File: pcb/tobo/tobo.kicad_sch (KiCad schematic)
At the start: 88 parts, among them J1 54548-2272, J2 Conn_01x02_Pin, J4 54548-2472, J5 Conn_01x09_Pin, J6 Conn_01x09_Pin, J7 Conn_01x09_Pin, J8 Hroparts Elec TYPE-C-31-M-12, U1 TS5A23167DCUR, U10 5015, U11 5015, U12 5015, U13 5015, U14 CH340E, U15 5015, U16 5015, U2 ATmega328P-AN, U3 TS5A23167DCUR, U4 TS5A23167DCUR, U5 TS5A23167DCUR, U6 5015, U7 5015, U8 5015, U9 5015, X1 TestPoint, X2 TestPoint, X7 TestPoint, Y4 TestPoint

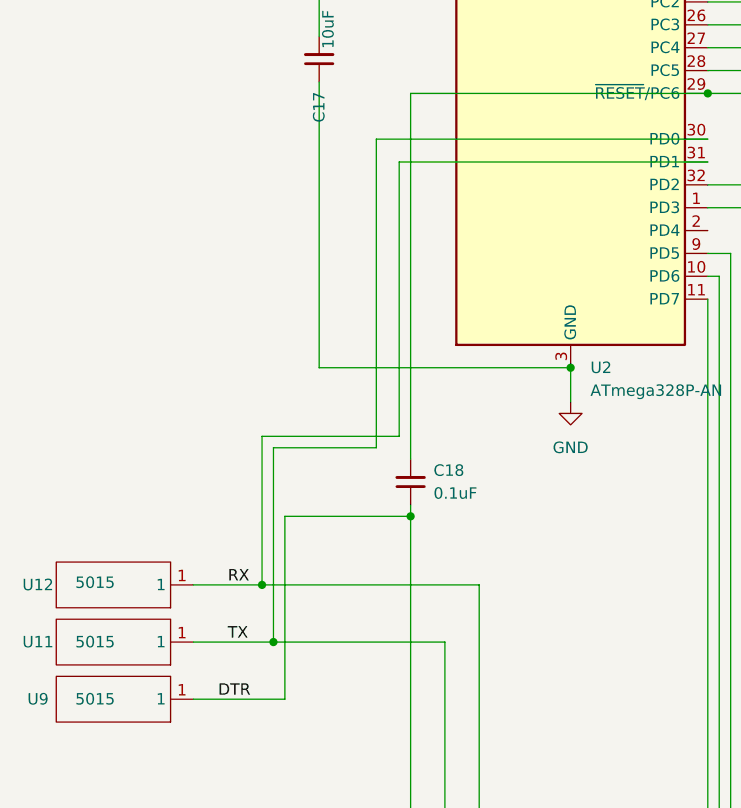
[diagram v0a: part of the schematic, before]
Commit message: Solution to the PCB error in v0.3a
If you've got a v0.4 board, no need to futz around with RX/TX.
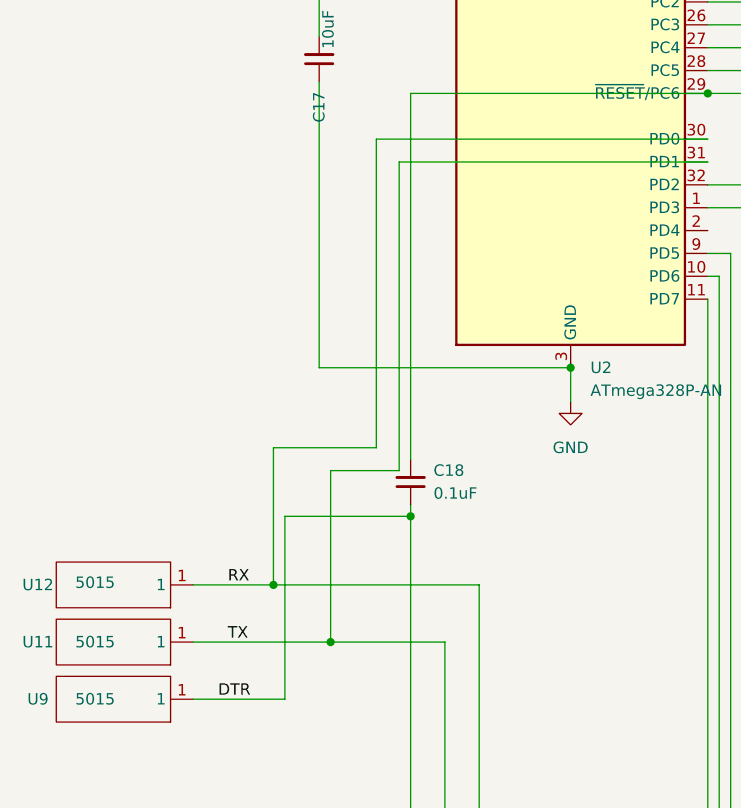
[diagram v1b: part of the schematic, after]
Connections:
- net RX: now also U2.30 (PD0); no longer U2.31 (PD1)
- net TX: now also U2.31 (PD1); no longer U2.30 (PD0)
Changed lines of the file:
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@@
+	)
+	(junction
+		(at 48.26 171.45)
+		(diameter 0)
+		(color 0 0 0 0)
 	)
 	(junction
@@
 	)
 	(junction
+		(at 41.91 165.1)
+		(diameter 0)
+		(color 0 0 0 0)
+	)
+	(junction
 		(at 331.47 201.93)
 		(diameter 0)
@@
 	)
 	(junction
-		(at 40.64 165.1)
-		(diameter 0)
-		(color 0 0 0 0)
-	)
-	(junction
 		(at 107.95 204.47)
 		(diameter 0)
@@
 		(color 0 0 0 0)
 	)
-	(junction
-		(at 41.91 171.45)
-		(diameter 0)
-		(color 0 0 0 0)
-	)
 	(wire
 		(pts
@@
 	(wire
 		(pts
-			(xy 40.64 148.59) (xy 40.64 165.1)
-		)
-		(stroke
-			(width 0)
-			(type default)
-		)
-	)
-	(wire
-		(pts
 			(xy 132.08 172.72) (xy 132.08 196.85)
 		)
@@
 	(wire
 		(pts
+			(xy 48.26 171.45) (xy 60.96 171.45)
+		)
+		(stroke
+			(width 0)
+			(type default)
+		)
+	)
+	(wire
+		(pts
 			(xy 327.66 170.18) (xy 327.66 187.96)
 		)
@@
 	(wire
 		(pts
-			(xy 40.64 148.59) (xy 55.88 148.59)
-		)
-		(stroke
-			(width 0)
-			(type default)
-		)
-	)
-	(wire
-		(pts
 			(xy 217.17 73.66) (xy 217.17 76.2)
 		)
@@
 	(wire
 		(pts
+			(xy 41.91 165.1) (xy 64.77 165.1)
+		)
+		(stroke
+			(width 0)
+			(type default)
+		)
+	)
+	(wire
+		(pts
 			(xy 186.69 63.5) (xy 189.23 63.5)
 		)
@@
 	(wire
 		(pts
-			(xy 41.91 171.45) (xy 60.96 171.45)
-		)
-		(stroke
-			(width 0)
-			(type default)
-		)
-	)
-	(wire
-		(pts
 			(xy 194.31 63.5) (xy 196.85 63.5)
 		)
@@
 	(wire
 		(pts
-			(xy 33.02 171.45) (xy 41.91 171.45)
+			(xy 33.02 171.45) (xy 48.26 171.45)
 		)
 		(stroke
@@
 	(wire
 		(pts
-			(xy 40.64 165.1) (xy 64.77 165.1)
+			(xy 33.02 165.1) (xy 41.91 165.1)
 		)
 		(stroke
@@
 	(wire
 		(pts
-			(xy 55.88 118.11) (xy 55.88 148.59)
+			(xy 55.88 118.11) (xy 55.88 152.4)
 		)
 		(stroke
@@
 	(wire
 		(pts
+			(xy 41.91 149.86) (xy 41.91 165.1)
+		)
+		(stroke
+			(width 0)
+			(type default)
+		)
+	)
+	(wire
+		(pts
 			(xy 137.16 100.33) (xy 110.49 100.33)
 		)
@@
 	(wire
 		(pts
-			(xy 33.02 165.1) (xy 40.64 165.1)
-		)
-		(stroke
-			(width 0)
-			(type default)
-		)
-	)
-	(wire
-		(pts
 			(xy 254 93.98) (xy 274.32 93.98)
 		)
@@
 	(wire
 		(pts
+			(xy 48.26 152.4) (xy 48.26 171.45)
+		)
+		(stroke
+			(width 0)
+			(type default)
+		)
+	)
+	(wire
+		(pts
 			(xy 134.62 228.6) (xy 134.62 237.49)
 		)
@@
 	(wire
 		(pts
-			(xy 41.91 149.86) (xy 41.91 171.45)
-		)
-		(stroke
-			(width 0)
-			(type default)
-		)
-	)
-	(wire
-		(pts
 			(xy 223.52 140.97) (xy 223.52 149.86)
 		)
@@
 		)
 		(stroke
+			(width 0)
+			(type default)
+		)
+	)
+	(wire
+		(pts
+			(xy 55.88 152.4) (xy 48.26 152.4)
+		)
+		(stroke

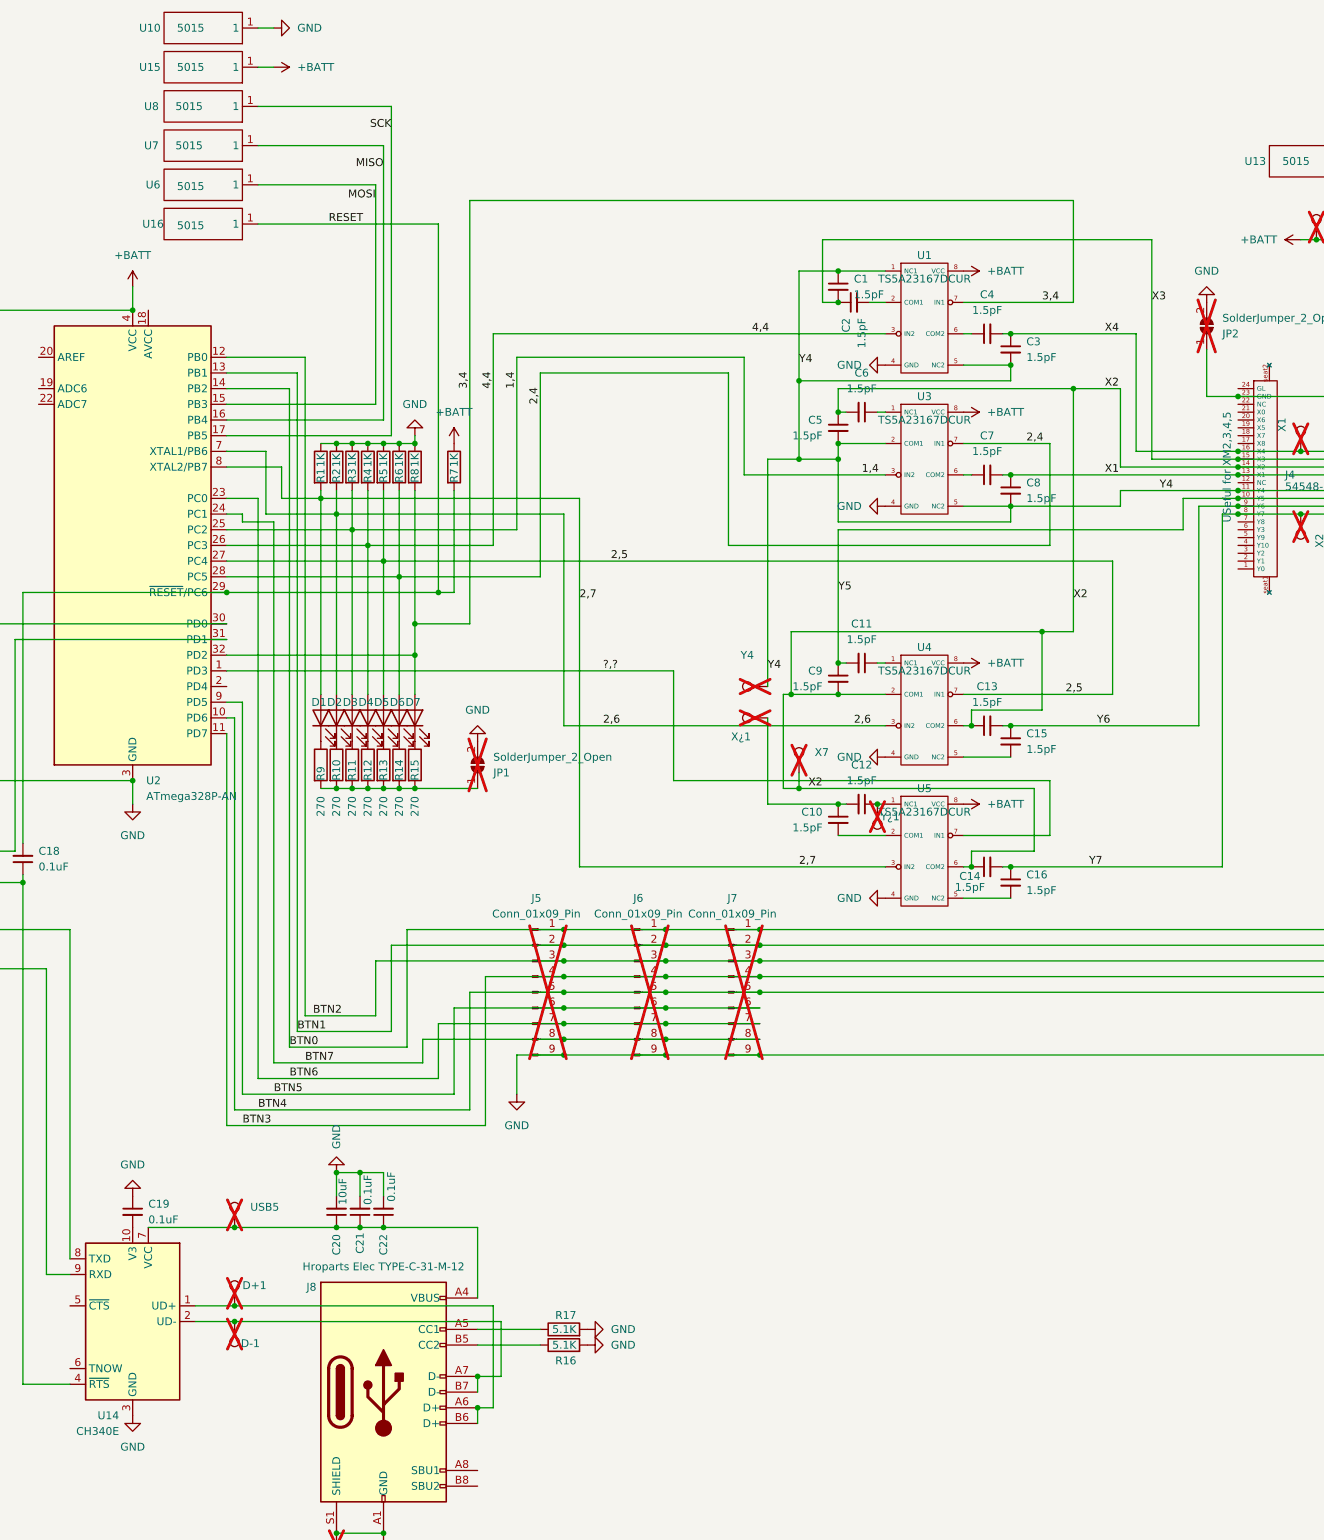
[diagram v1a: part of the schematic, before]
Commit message: PCB: Bump to Kicad 9 and preparation for step-up transformer
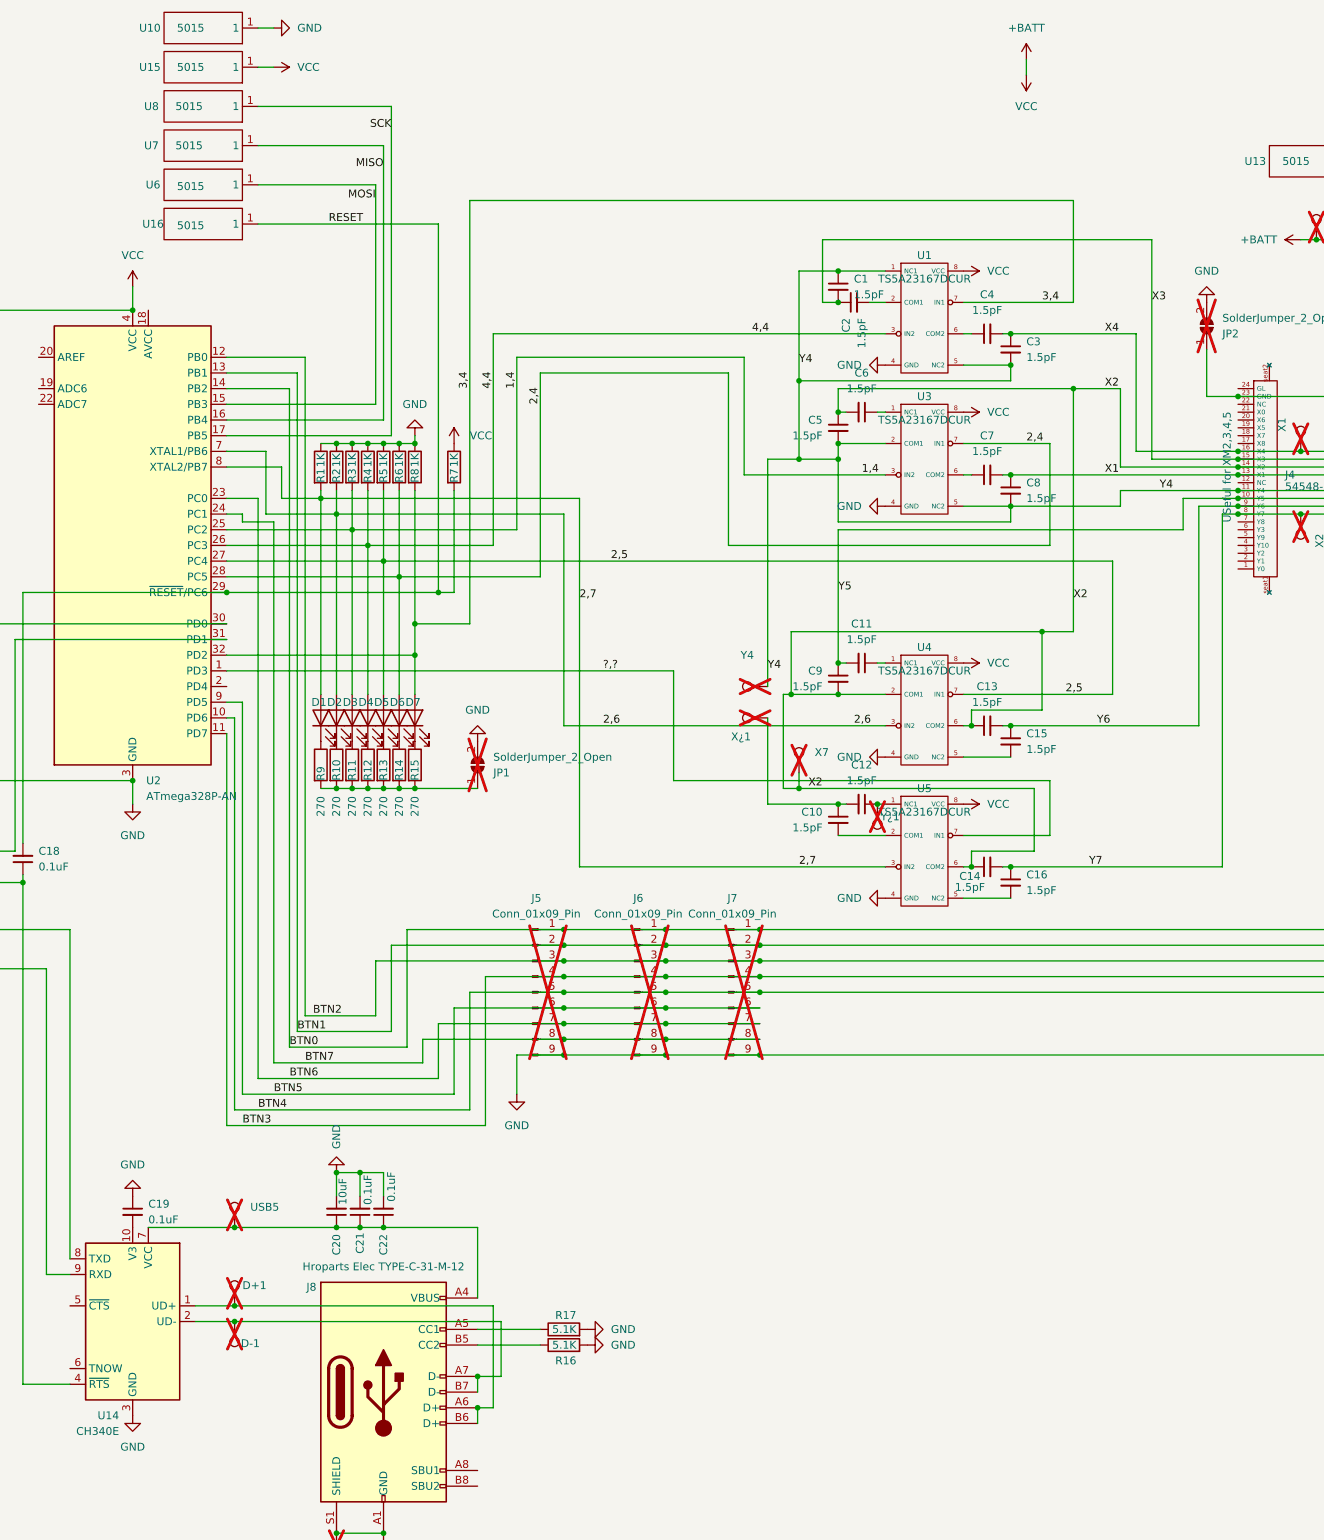
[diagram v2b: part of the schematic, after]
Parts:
- J1: value 54548-2272 -> 54548-2272
- U1, U3, U4, U5: footprint Package_SO:VSSOP-8_2.3x2mm_P0.5mm -> tobo-footprints:VSSOP-8_2.3x2mm_P0.5mm_narrowpads
- U14: footprint Package_SO:MSOP-10_3x3mm_P0.5mm -> tobo-footprints:MSOP-10_3x3mm_P0.5mm_narrowpads

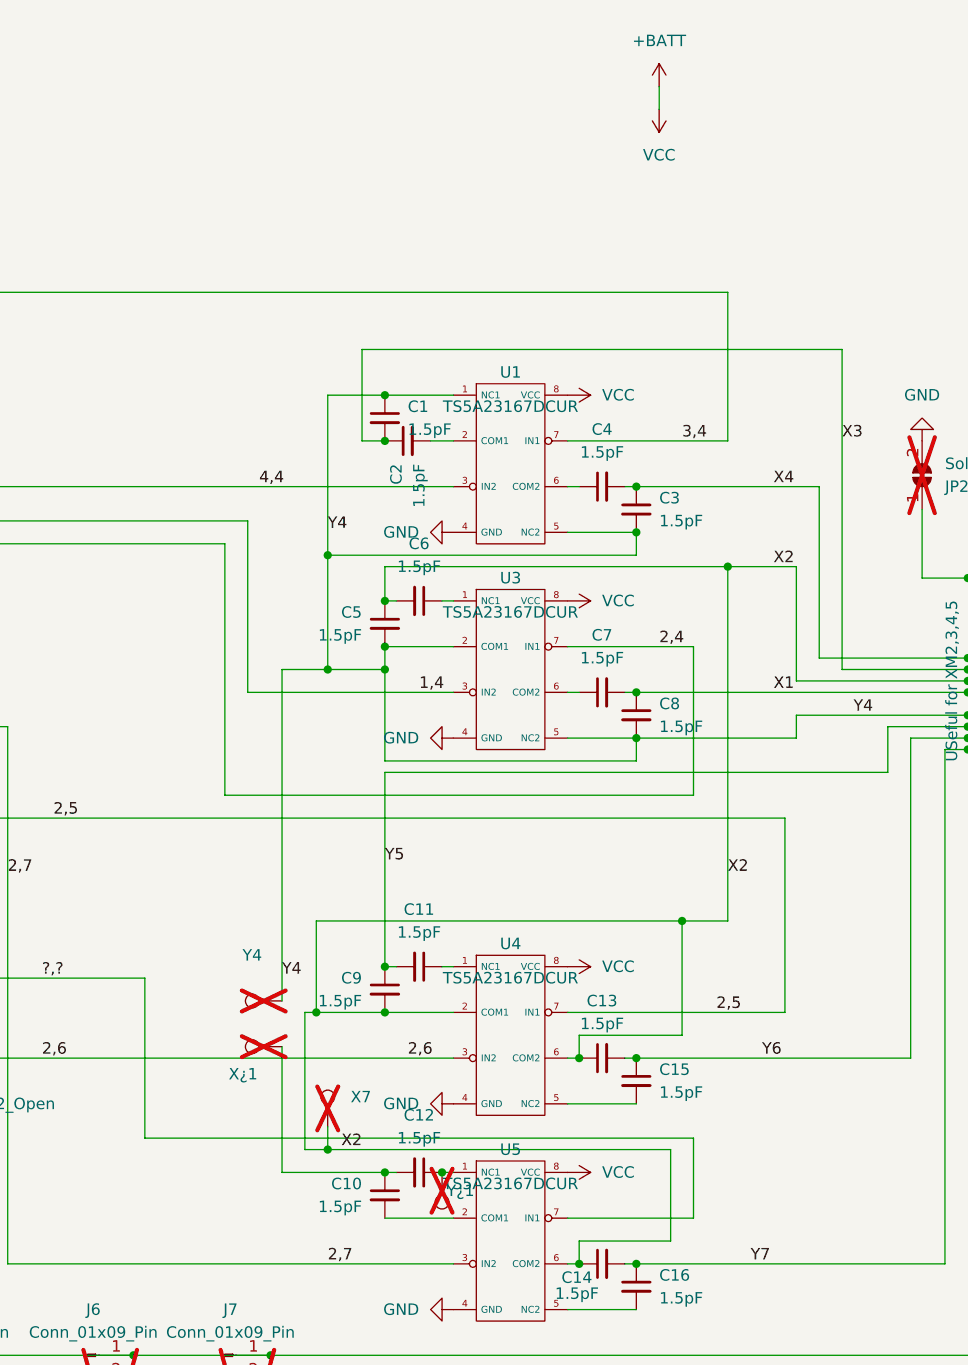
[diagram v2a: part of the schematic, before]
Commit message: First stab at a step-up converter on the tobo
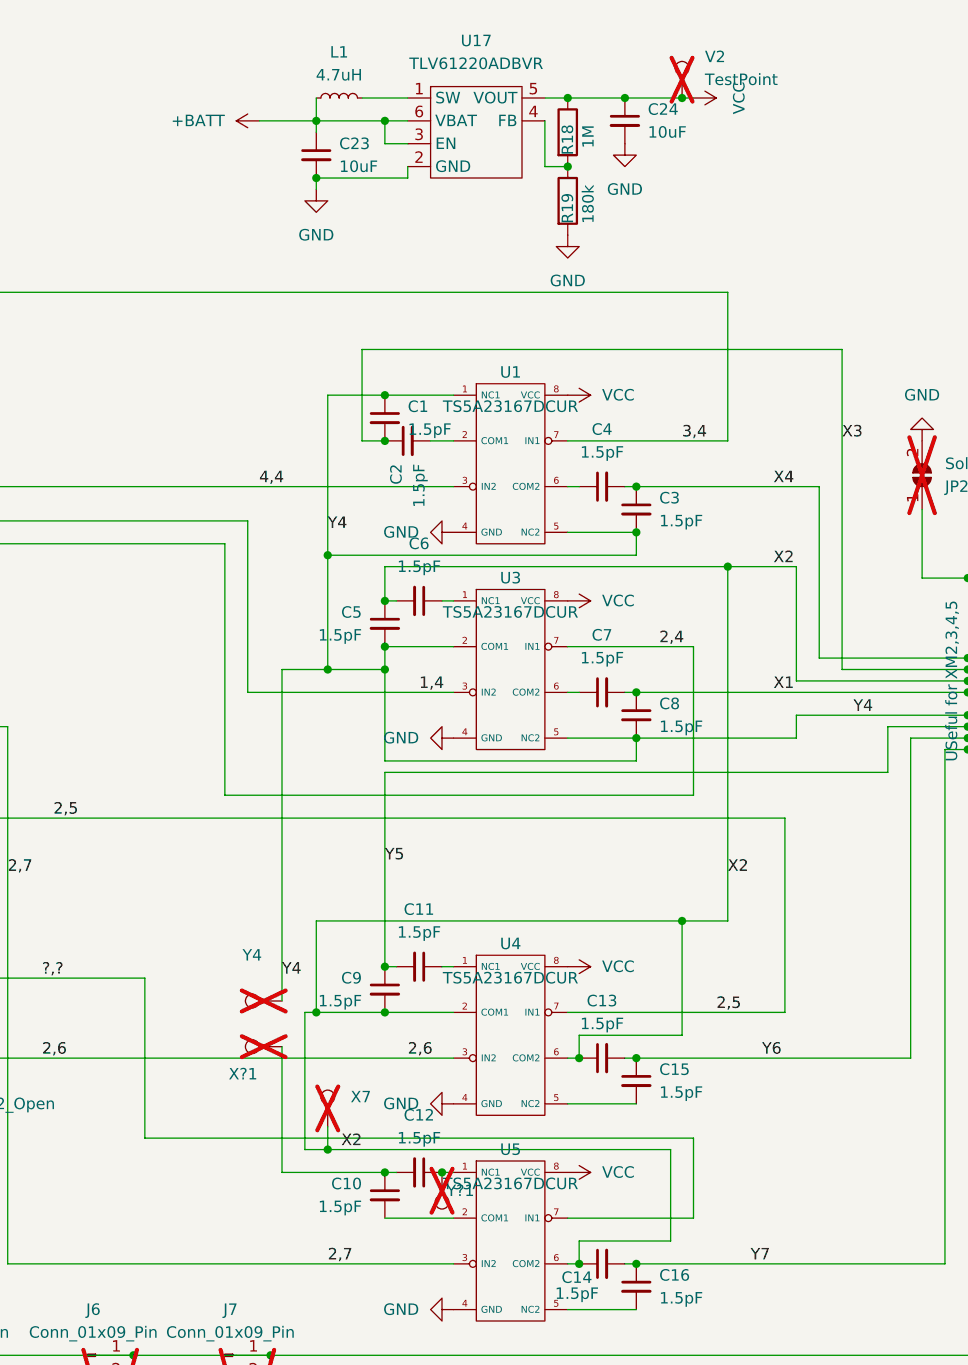
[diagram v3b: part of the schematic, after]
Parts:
- added C23, C24: 10uF, Capacitor_SMD:C_0402_1005Metric, symbol Device:C_Small
- added L1: 4.7uH, Inductor_SMD:L_1008_2520Metric, symbol Device:L_Small
- added R18: 1M, Resistor_SMD:R_0201_0603Metric, symbol Device:R
- added R19: 180k, Resistor_SMD:R_0201_0603Metric, symbol Device:R
- added U17: TLV61220ADBVR, Package_TO_SOT_SMD:SOT-23-6, symbol tobo-components:TLV61220A
- added V2: TestPoint, TestPoint:TestPoint_Pad_D1.0mm, symbol Connector:TestPoint
- renumbered X¿1 to X?1, Y¿1 to Y?1
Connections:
- net +BATT: now also C23.1, L1.1, U17.3 (EN), U17.6 (VBAT); no longer C17.2, R7.1, U1.8 (VCC), U15.1, U2.4 (VCC), U2.6 (VCC), U3.8 (VCC), U4.8 (VCC), U5.8 (VCC)
- net GND: now also C23.2, C24.2, R19.2, U17.2 (GND)
- new net: L1.2, U17.1 (SW)
- new net: R18.2, R19.1, U17.4 (FB)
- new net VCC: C17.2, C24.1, R18.1, R7.1, U1.8 (VCC), U15.1, U17.5 (VOUT), U2.4 (VCC), U2.6 (VCC), U3.8 (VCC), U4.8 (VCC), U5.8 (VCC), V2.1
